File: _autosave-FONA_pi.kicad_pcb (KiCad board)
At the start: 2 copper layers, 88.4 x 59.1 mm, 37 parts, among them J1 Conn_01x20_Socket, J10 Conn_01x04_Pin, J11 Conn_01x20_Socket, J12 Conn_01x20_Socket, J13 Conn_01x06_Socket, J14 Conn_01x06_Socket, J15 Conn_01x06_Socket, J16 Conn_01x06_Socket, J17 Conn_01x06_Socket, J18 Conn_01x04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

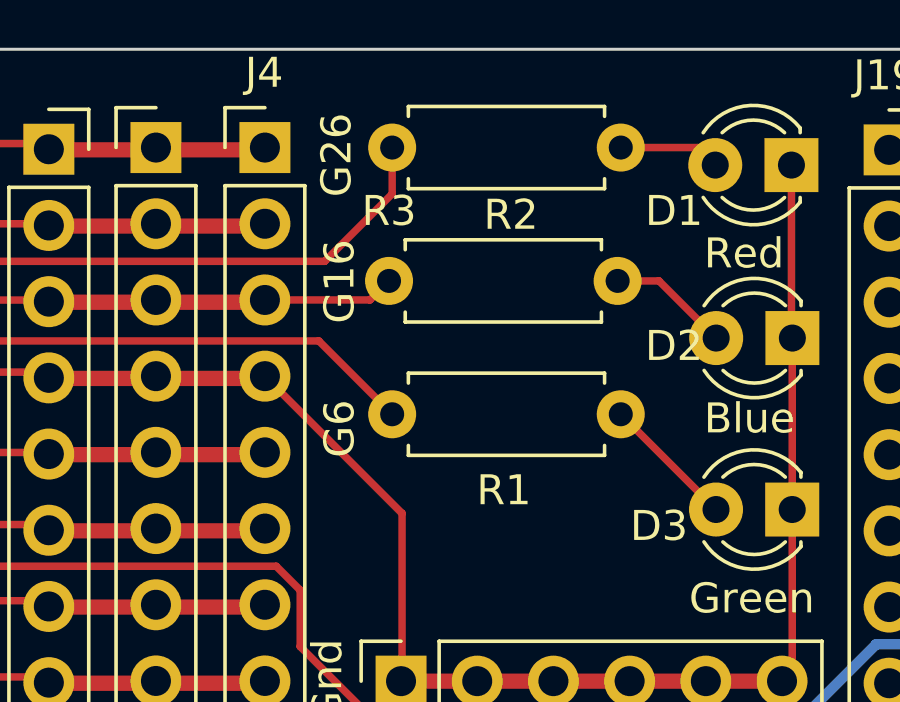
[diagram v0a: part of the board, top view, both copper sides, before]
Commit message: Flipped a backwards resistor.  Added labels for LED colors, switch resistors
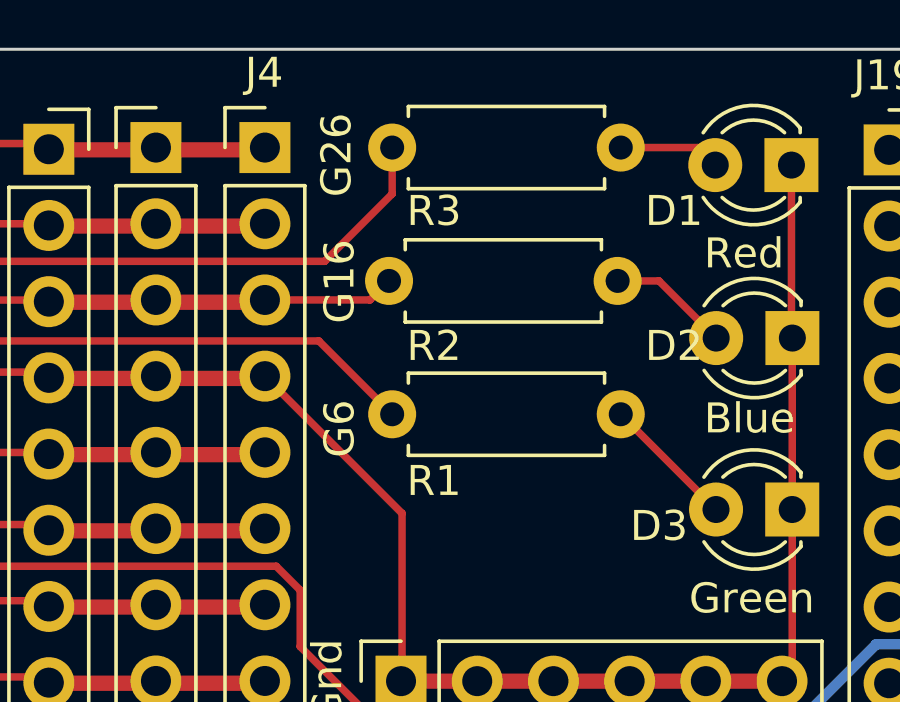
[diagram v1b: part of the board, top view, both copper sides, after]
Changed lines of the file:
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@@
     (property "ki_keywords" "R res resistor")
     (attr through_hole)
-    (fp_text reference "R1" (at 3.7256 2.5362) (layer "F.SilkS")
+    (fp_text reference "R1" (at 1.3956 2.2262) (layer "F.SilkS")
         (effects (font (size 1 1) (thickness 0.15)))
     )
@@
     (property "ki_keywords" "R res resistor")
     (attr through_hole)
-    (fp_text reference "R3" (at -0.1044 2.1162) (layer "F.SilkS")
+    (fp_text reference "R3" (at 1.3956 2.1162) (layer "F.SilkS")
         (effects (font (size 1 1) (thickness 0.15)))
     )
@@
     (property "ki_keywords" "R res resistor")
     (attr through_hole)
-    (fp_text reference "R2" (at 4.0644 -2.2012) (layer "F.SilkS")
-        (effects (font (size 1 1) (thickness 0.15)))
-    )
+    (fp_text reference "R2" (at 1.5 2.1712) (layer "F.SilkS")
+        (effects (font (size 1 1) (thickness 0.15)))
+    )
